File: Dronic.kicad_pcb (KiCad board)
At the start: 2 copper layers, 8.6 x 5.3 mm, 52 parts, among them J1 Screw_Terminal_01x02, J2 Screw_Terminal_01x02, U1 RP2040, U2 2137160001, U3 W25Q128JVS, U4 LTC3521EFE-PBF, U5 AP62150WU, U6 ECH8690-TL-H, U7 ECH8690-TL-H, Y1 ABM3B-12.000MHZ-10-1-U-T

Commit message: SM06B-SRSS-TB 6 Pin Connector Male, this will be used for the Benewake TFS20-L LiDAR Module
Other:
- copper layers 2 -> 4
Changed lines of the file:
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@@
 	(paper "A4")
 	(layers
-		(0 "F.Cu" signal)
-		(2 "B.Cu" signal)
+		(0 "F.Cu" signal "L1.Cu")
+		(4 "In1.Cu" signal "L2.Cu")
+		(6 "In2.Cu" signal "L3.Cu")
+		(2 "B.Cu" signal "L4.Cu")
 		(9 "F.Adhes" user "F.Adhesive")
 		(11 "B.Adhes" user "B.Adhesive")
@@
 	)
 	(setup
+		(stackup
+			(layer "F.SilkS"
+				(type "Top Silk Screen")
+			)
+			(layer "F.Paste"
+				(type "Top Solder Paste")
+			)
+			(layer "F.Mask"
+				(type "Top Solder Mask")
+				(thickness 0.01)
+			)
+			(layer "F.Cu"
+				(type "copper")
+				(thickness 0.035)
+			)
+			(layer "dielectric 1"
+				(type "prepreg")
+				(thickness 0.1)
+				(material "FR4")
+				(epsilon_r 4.5)
+				(loss_tangent 0.02)
+			)
+			(layer "In1.Cu"
+				(type "copper")
+				(thickness 0.035)
+			)
+			(layer "dielectric 2"
+				(type "core")
+				(thickness 1.24)
+				(material "FR4")
+				(epsilon_r 4.5)
+				(loss_tangent 0.02)
+			)
+			(layer "In2.Cu"
+				(type "copper")
+				(thickness 0.035)
+			)
+			(layer "dielectric 3"
+				(type "prepreg")
+				(thickness 0.1)
+				(material "FR4")
+				(epsilon_r 4.5)
+				(loss_tangent 0.02)
+			)
+			(layer "B.Cu"
+				(type "copper")
+				(thickness 0.035)
+			)
+			(layer "B.Mask"
+				(type "Bottom Solder Mask")
+				(thickness 0.01)
+			)
+			(layer "B.Paste"
+				(type "Bottom Solder Paste")
+			)
+			(layer "B.SilkS"
+				(type "Bottom Silk Screen")
+			)
+			(copper_finish "None")
+			(dielectric_constraints no)
+		)
 		(pad_to_mask_clearance 0)
 		(allow_soldermask_bridges_in_footprints no)
@@
 			(psa4output no)
 			(plot_black_and_white yes)
-			(plotinvisibletext no)
 			(sketchpadsonfab no)
 			(plotpadnumbers no)

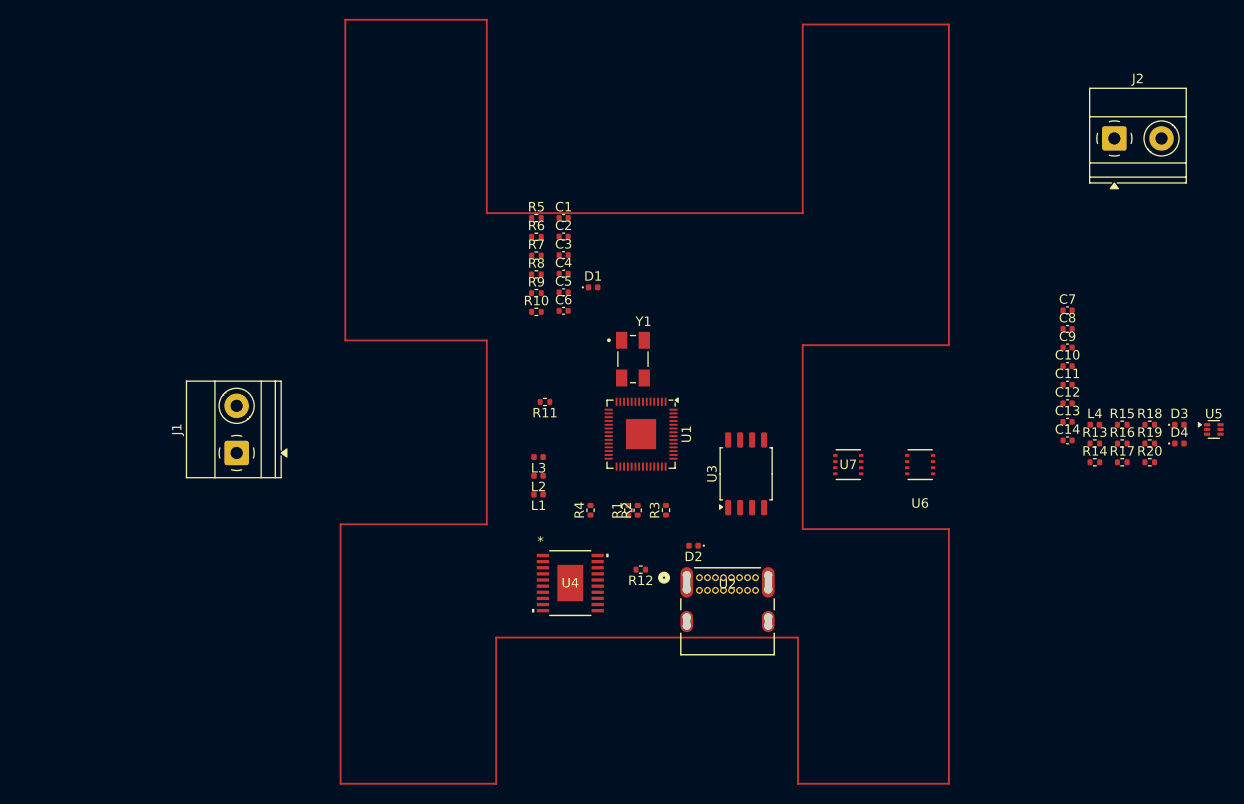
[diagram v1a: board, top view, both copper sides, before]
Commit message: Added new parts, Edited Schematic
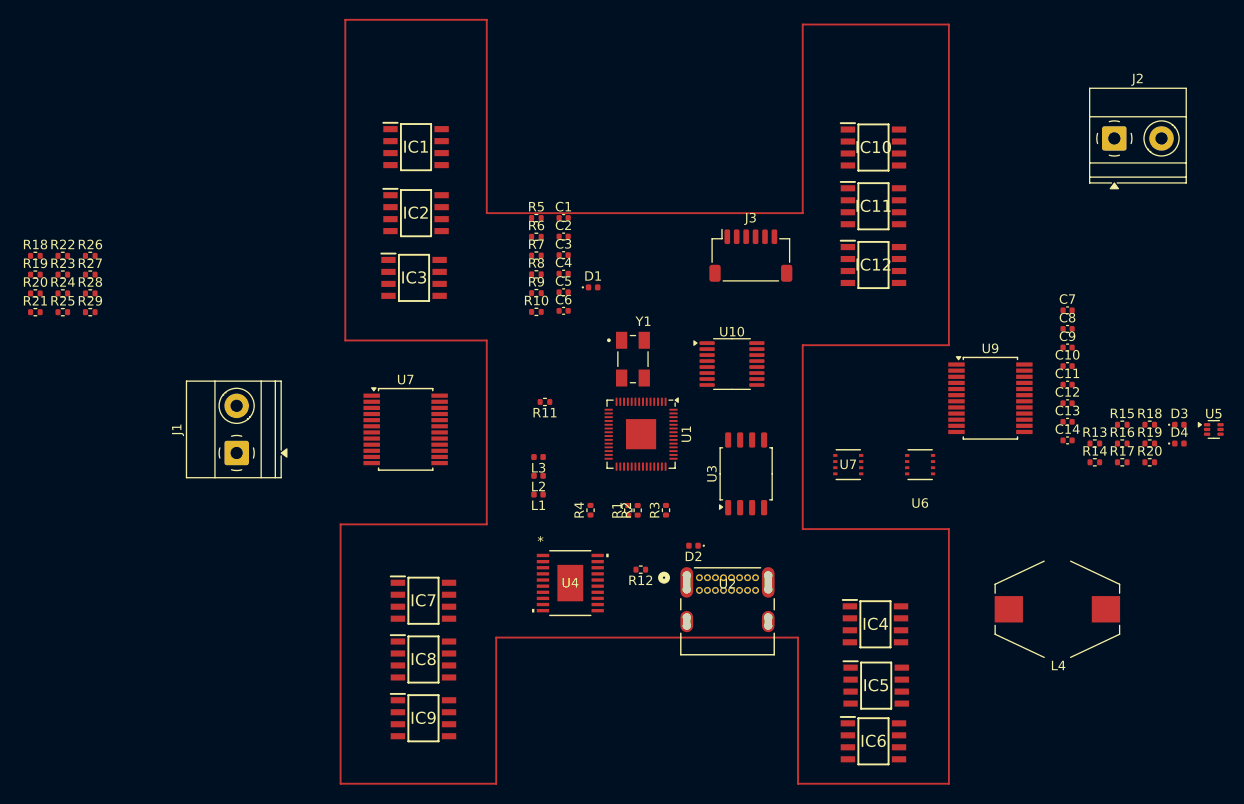
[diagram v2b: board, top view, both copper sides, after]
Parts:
- added IC1: ACS71240LLCBTR-050U5, ACS71240LLCBTR-050U5:SOIC127P600X175-8N, F.Cu at (92.5, 69.5)
- added IC10: ACS71240LLCBTR-050U5, ACS71240LLCBTR-050U5:SOIC127P600X175-8N, F.Cu at (141.0, 69.5)
- added IC11: ACS71240LLCBTR-050U5, ACS71240LLCBTR-050U5:SOIC127P600X175-8N, F.Cu at (141.0, 75.8)
- added IC12: ACS71240LLCBTR-050U5, ACS71240LLCBTR-050U5:SOIC127P600X175-8N, F.Cu at (141.0, 82.0)
- added IC2: ACS71240LLCBTR-050U5, ACS71240LLCBTR-050U5:SOIC127P600X175-8N, F.Cu at (92.5, 76.5)
- added IC3: ACS71240LLCBTR-050U5, ACS71240LLCBTR-050U5:SOIC127P600X175-8N, F.Cu at (92.3, 83.4)
- added IC4: ACS71240LLCBTR-050U5, ACS71240LLCBTR-050U5:SOIC127P600X175-8N, F.Cu at (141.2, 120.1)
- added IC5: ACS71240LLCBTR-050U5, ACS71240LLCBTR-050U5:SOIC127P600X175-8N, F.Cu at (141.3, 126.6)
- added IC6: ACS71240LLCBTR-050U5, ACS71240LLCBTR-050U5:SOIC127P600X175-8N, F.Cu at (141.0, 132.5)
- added IC7: ACS71240LLCBTR-050U5, ACS71240LLCBTR-050U5:SOIC127P600X175-8N, F.Cu at (93.3, 117.6)
- added IC8: ACS71240LLCBTR-050U5, ACS71240LLCBTR-050U5:SOIC127P600X175-8N, F.Cu at (93.3, 123.8)
- added IC9: ACS71240LLCBTR-050U5, ACS71240LLCBTR-050U5:SOIC127P600X175-8N, F.Cu at (93.3, 130.1)
- added J3: JST_SH_6P_1.00mm, Connector_JST:JST_SH_SM06B-SRSS-TB_1x06-1MP_P1.00mm_Horizontal, F.Cu at (128.0, 81.0)
- added R18: 10K, Resistor_SMD:R_0402_1005Metric, F.Cu at (52.1, 81.0)
- added R19: 10K, Resistor_SMD:R_0402_1005Metric, F.Cu at (52.1, 83.0)
- added R20: 5K, Resistor_SMD:R_0402_1005Metric, F.Cu at (52.1, 85.0)
- added R21: 5K, Resistor_SMD:R_0402_1005Metric, F.Cu at (52.1, 87.0)
- added R22: 5K, Resistor_SMD:R_0402_1005Metric, F.Cu at (55.0, 81.0)
- added R23: 5K, Resistor_SMD:R_0402_1005Metric, F.Cu at (55.0, 83.0)
- added R24: 5K, Resistor_SMD:R_0402_1005Metric, F.Cu at (55.0, 85.0)
- added R25: 5K, Resistor_SMD:R_0402_1005Metric, F.Cu at (55.0, 87.0)
- added R26: 5K, Resistor_SMD:R_0402_1005Metric, F.Cu at (58.0, 81.0)
- added R27: 5K, Resistor_SMD:R_0402_1005Metric, F.Cu at (58.0, 83.0)
- added R28: 5K, Resistor_SMD:R_0402_1005Metric, F.Cu at (58.0, 85.0)
- added R29: 5K, Resistor_SMD:R_0402_1005Metric, F.Cu at (58.0, 87.0)
- added U10: MAX11616, Package_SO:QSOP-16_3.9x4.9mm_P0.635mm, F.Cu at (126.0, 92.5)
- added U7: PCF8575DBR, Package_SO:SSOP-24_5.3x8.2mm_P0.65mm, F.Cu at (91.4, 99.4)
- added U9: PCF8575DBR, Package_SO:SSOP-24_5.3x8.2mm_P0.65mm, F.Cu at (153.4, 96.1)
- C1, C2: value 22uF -> 10uF
- C3: value 22uF -> 28uF
- J1: value Screw_Terminal_01x02 -> SWDIO_PH_TERM
- L4: value 3.3uH -> 68uH; footprint Inductor_SMD:L_0402_1005Metric -> Inductor_SMD:L_Bourns-SRR1005
- R10: value 5.1K -> 1.0M
- R15: value 5.1K -> 52.3K
- R16: value 5.1K -> 10K
- R5: value 5.1K -> 137K
- R6: value 5.1K -> 68.1K
- R7: value 5.1K -> 100k
- R8: value 5.1K -> 100K
- R9: value 5.1K -> 221K
- moved L4 20.0 mm to (160.5, 118.5)
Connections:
- D1 pad 2: VBUS -> VDD
- R11 pad 1: +1.8V -> +3.3V
- R11 pad 2: VCC -> Net-(U8-GATE1)
- R12 pad 2: VCC -> Net-(U8-GATE2)
- U1 pad 11: unconnected-(U1-GPIO8-Pad11) -> SDA
- U1 pad 12: unconnected-(U1-GPIO9-Pad12) -> SCL
- U1 pad 13: unconnected-(U1-GPIO10-Pad13) -> TFS20_CS
- U1 pad 26: unconnected-(U1-RUN-Pad26) -> Net-(U1-RUN)
- U6 pad 4: Net-(U6-Gate2) -> VBAT_REG_INVERTED
- U6 pad 5: VCC -> VDD
- U6 pad 6: VCC -> VDD
- U6 pad 7: unconnected-(U6-Drain1-Pad7) -> VDD
- U6 pad 8: VCC -> VDD
